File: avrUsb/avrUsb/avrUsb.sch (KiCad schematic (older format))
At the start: 15 parts, among them J1 Screw_Terminal_01x07, J2 Screw_Terminal_01x10, J3 Screw_Terminal_01x10, U1 ATmega8U2-AU, X1 USBFCI_10103594, Y1 8 Mhz

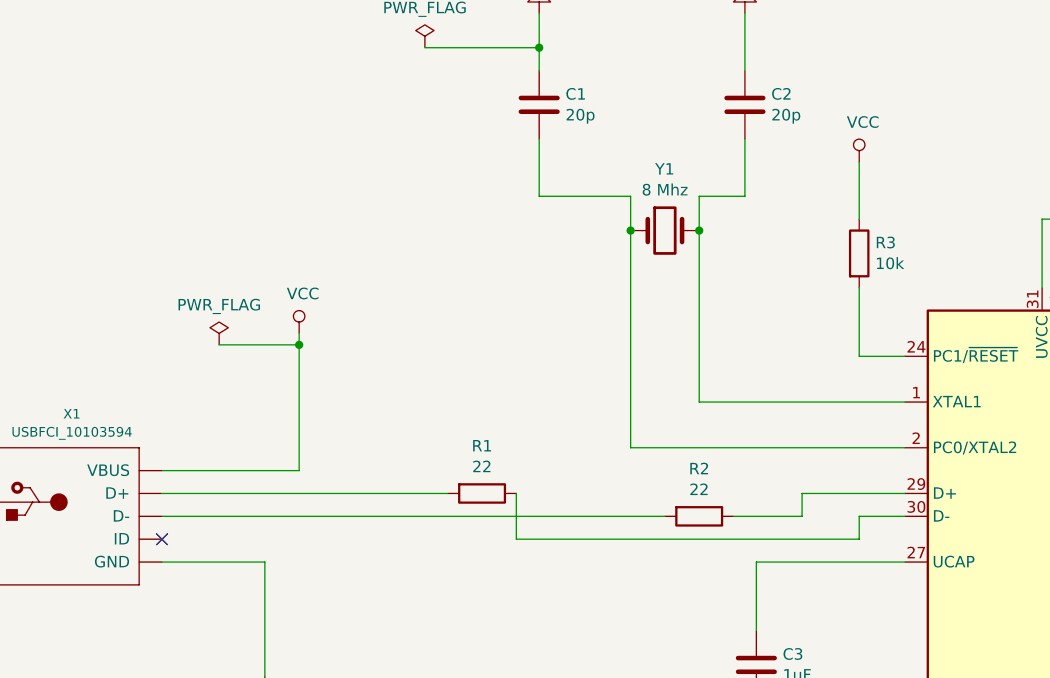
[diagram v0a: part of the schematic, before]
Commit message: updated usb polarity + reset header
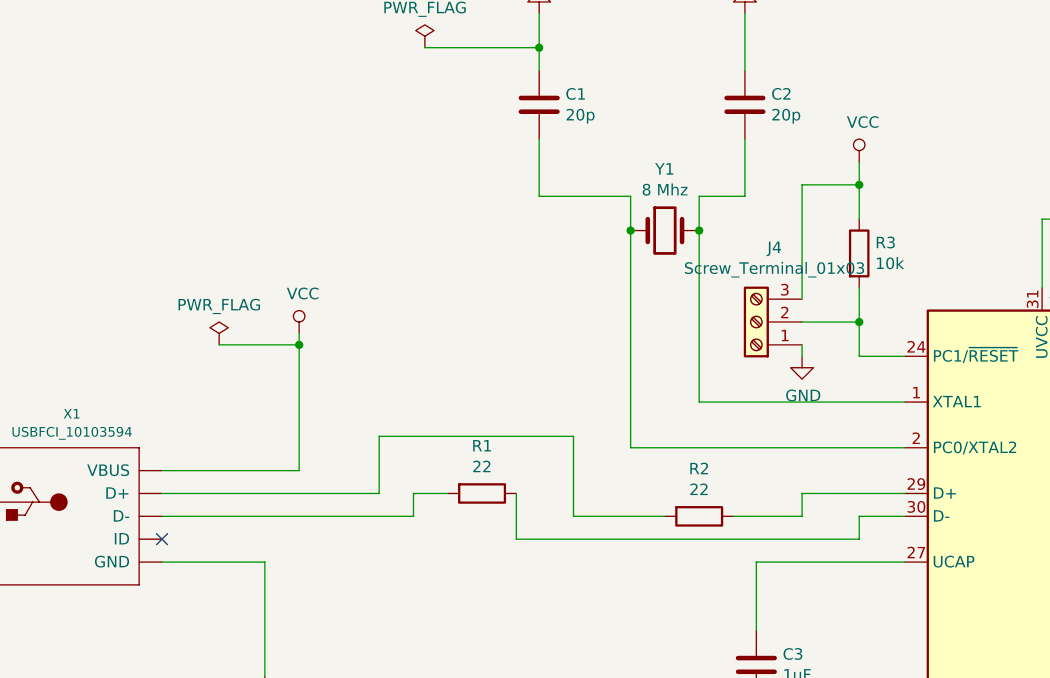
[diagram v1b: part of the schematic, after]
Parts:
- added J4: Screw_Terminal_01x03, TerminalBlock_Phoenix:TerminalBlock_Phoenix_MPT-0,5-3-2.54_1x03_P2.54mm_Horizontal, symbol Connector:Screw_Terminal_01x03
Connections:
- net GND: now also J4.1 (Pin_1)
- net VCC: now also J4.3 (Pin_3)
- net at X1.D+: now also R2.2; no longer R1.2
- net at X1.D-: now also R1.2; no longer R2.2
- net at R3.2, U1.24 (PC1/~RESET): now also J4.2 (Pin_2)
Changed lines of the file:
@@
 	0    1    1    0
 $EndComp
-Wire Wire Line
-	2000 2950 4200 2950
-Wire Wire Line
-	2000 2850 3250 2850
 $Comp
 L avrUsb-rescue:ATmega8U2-AU-MCU_Microchip_ATmega U1
@@
 $EndComp
 Wire Wire Line
-	5050 1400 5050 1650
-Wire Wire Line
-	5050 1950 5050 2250
+	5050 1400 5050 1500
+Wire Wire Line
+	5050 1950 5050 2100
 Wire Wire Line
 	7150 2050 7150 1900
@@
 Wire Wire Line
 	5050 2950 5250 2950
+$Comp
+L Connector:Screw_Terminal_01x03 J4
+U 1 1 5CE71C0B
+P 4600 2100
+F 0 "J4" H 4520 1775 50  0000 C CNN
+F 1 "Screw_Terminal_01x03" H 4520 1866 50  0000 C CNN
+F 2 "TerminalBlock_Phoenix:TerminalBlock_Phoenix_MPT-0,5-3-2.54_1x03_P2.54mm_Horizontal" H 4600 2100 50  0001 C CNN
+F 3 "~" H 4600 2100 50  0001 C CNN
+	1    4600 2100
+	-1   0    0    1
+$EndComp
+Wire Wire Line
+	4800 2100 5050 2100
+Connection ~ 5050 2100
+Wire Wire Line
+	5050 2100 5050 2250
+Wire Wire Line
+	5050 1500 4800 1500
+Wire Wire Line
+	4800 1500 4800 2000
+Connection ~ 5050 1500
+Wire Wire Line
+	5050 1500 5050 1650
+$Comp
+L power:GND #PWR016
+U 1 1 5CE7BBCA
+P 4800 2250
+F 0 "#PWR016" H 4800 2000 50  0001 C CNN
+F 1 "GND" H 4805 2077 50  0000 C CNN
+F 2 "" H 4800 2250 50  0001 C CNN
+F 3 "" H 4800 2250 50  0001 C CNN
+	1    4800 2250
+	1    0    0    -1
+$EndComp
+Wire Wire Line
+	4800 2200 4800 2250
+Wire Wire Line
+	2000 2850 2950 2850
+Wire Wire Line
+	2950 2850 2950 2600
+Wire Wire Line
+	2950 2600 3800 2600
+Wire Wire Line
+	3800 2600 3800 2950
+Wire Wire Line
+	3800 2950 4200 2950
+Wire Wire Line
+	2000 2950 3100 2950
+Wire Wire Line
+	3100 2950 3100 2850
+Wire Wire Line
+	3100 2850 3250 2850
 $EndSCHEMATC

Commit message: QFN
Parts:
- removed U1: ATmega8U2-AU, QFP:TQFP-32_7x7mm_P0.8mm, symbol avrUsb-rescue:ATmega8U2-AU-MCU_Microchip_ATmega
- added U1: ATmega32U2-MU, Package_DFN_QFN:QFN-32-1EP_5x5mm_P0.5mm_EP3.1x3.1mm, symbol MCU_Microchip_ATmega:ATmega32U2-MU
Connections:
- net GND: now also U1.28 (UGND), U1.3 (GND), U1.33 (GND)
- net VCC: now also U1.31 (UVCC), U1.32 (AVCC), U1.4 (VCC)
- net at R1.1: now also U1.30 (D-)
- net at R2.1: now also U1.29 (D+)
- net at C2.2, Y1.2: now also U1.1 (XTAL1)
- net at J3.5 (Pin_5): now also U1.22 (PC7)
- net at J3.6 (Pin_6): now also U1.6 (PD0)
- net at J3.7 (Pin_7): now also U1.7 (PD1)
- net at J3.8 (Pin_8): now also U1.8 (PD2)
- net at J2.1 (Pin_1): now also U1.14 (PB0)
- net at J2.2 (Pin_2): now also U1.15 (PB1)
- net at J2.3 (Pin_3): now also U1.16 (PB2)
- net at J2.4 (Pin_4): now also U1.17 (PB3)
- net at J2.5 (Pin_5): now also U1.18 (PB4)
- net at J2.6 (Pin_6): now also U1.19 (PB5)
- net at C1.2, Y1.1: now also U1.2 (PC0/XTAL2)
- net at J2.7 (Pin_7): now also U1.20 (PB6)
- net at J2.8 (Pin_8): now also U1.21 (PB7)
- net at J1.5 (Pin_5): now also U1.13 (~HWB~/PD7)
- net at J1.4 (Pin_4): now also U1.12 (PD6)
- net at J4.2 (Pin_2), R3.2: now also U1.24 (PC1/~RESET)
- net at J1.3 (Pin_3): now also U1.11 (PD5)
- net at J1.2 (Pin_2): now also U1.10 (PD4)
- net at C3.1: now also U1.27 (UCAP)
- net at J1.1 (Pin_1): now also U1.9 (PD3)
- net at J3.1 (Pin_1): now also U1.5 (PC2)
- net at J3.2 (Pin_2): now also U1.26 (PC4)
- net at J3.3 (Pin_3): now also U1.25 (PC5)
- net at J3.4 (Pin_4): now also U1.23 (PC6)
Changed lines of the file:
@@
-$EndComp
-$Comp
-L avrUsb-rescue:ATmega8U2-AU-MCU_Microchip_ATmega U1
-U 1 1 5BC9A81C
-P 5950 3350
-F 0 "U1" H 5950 1864 50  0000 C CNN
-F 1 "ATmega8U2-AU" H 5950 1773 50  0000 C CNN
-F 2 "QFP:TQFP-32_7x7mm_P0.8mm" H 5950 3350 50  0001 C CIN
-F 3 "http://ww1.microchip.com/downloads/en/DeviceDoc/doc7799.pdf" H 5950 3350 50  0001 C CNN
-	1    5950 3350
-	1    0    0    -1
 $EndComp
 $Comp
@@
 	7550 3550 7550 3600
 Wire Wire Line
-	6650 3750 7050 3750
-Wire Wire Line
-	7050 3750 7050 3700
-Wire Wire Line
 	7050 3700 7550 3700
-Wire Wire Line
-	6650 3850 7200 3850
-Wire Wire Line
-	7200 3850 7200 3800
 Wire Wire Line
 	7200 3800 7550 3800
@@
 Wire Wire Line
 	3100 2850 3250 2850
+$Comp
+L MCU_Microchip_ATmega:ATmega32U2-MU U1
+U 1 1 5D3054B2
+P 5950 3350
+F 0 "U1" H 5950 1864 50  0000 C CNN
+F 1 "ATmega32U2-MU" H 5950 1773 50  0000 C CNN
+F 2 "Package_DFN_QFN:QFN-32-1EP_5x5mm_P0.5mm_EP3.1x3.1mm" H 5950 3350 50  0001 C CIN
+F 3 "http://ww1.microchip.com/downloads/en/DeviceDoc/doc7799.pdf" H 5950 3350 50  0001 C CNN
+	1    5950 3350
+	1    0    0    -1
+$EndComp
+Wire Wire Line
+	7200 3800 7200 3950
+Wire Wire Line
+	6650 3950 7200 3950
+Wire Wire Line
+	6650 3850 7050 3850
+Wire Wire Line
+	7050 3700 7050 3850
+Wire Wire Line
+	6650 3750 6650 3650
 $EndSCHEMATC
